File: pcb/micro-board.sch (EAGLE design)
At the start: 100 parts, among them IC1 STM32F401RET6U, IC2 LDS3985M33R, IC3 LDS3985M33R, IC4 HX711, IC5 TLV2462IP, J12 B2B-PH-K-S_LF__SN_, J3 Button / ADC Header, Q1 S8550, Q2 16MHz, U1 MCP73831.SOT23-5

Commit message: Updated the PCB board and schematic. In process of generally laying down components. Will be working on the design for next 1.5 hours.
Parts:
- added J18: DC Power, LinnesLab-Connectors:CONN_02
- added R34, R35: 1.5, LinnesLab-Passives:RESISTOR0603
- added U$2: TP3, LinnesLab-Connectors:PAD
- added U$3: TP4, LinnesLab-Connectors:PAD
- added U$4: TP5, LinnesLab-Connectors:PAD
- added U$5: TP6, LinnesLab-Connectors:PAD
- added U$6: TP1, LinnesLab-Connectors:PAD
- added U$7: TP0, LinnesLab-Connectors:PAD
- added U$8: TP2, LinnesLab-Connectors:PAD
- J14: value (none) -> Digital LED
- J15: value (none) -> Analog LED
- J16: value (none) -> HX711 LED
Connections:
- new net BOOT0: IC1.BOOT0, R11.1, U$4.1
- new net N$19: IC2.VO, R34.2
- net 3.3V: now also R34.1, U$7.1, U$8.1; no longer IC2.VO
- net 5V: now also J18.2
- net GND: now also J18.1
- net HXCLK_P: now also U$2.1
- net HXDATA_P: now also U$3.1
- net N$15: now also IC3.VO, R35.2; no longer IC1.BOOT0, R11.1
- net NRST: now also U$5.1
- net VDDA: now also R35.1, U$6.1; no longer IC3.VO
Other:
- note added: "3V3 TP0"
- note added: "HX711: TP2"
- note added: "Power Debug LEDs (J14-J16: Shorted = Enabled)"
- note added: "VDDA TP1"
- note removed: "Power Debug LEDs (Jumper-Enabled)"
- note removed: "TODO: Add 1.5 ohm resistor in series with power supply."
- note removed: "TODO: Discuss 5V connector mount"
- moved on the sheet: C15, C16, C17, C19, C2, C20, C22, C23, C24, C3, C7, C8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

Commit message: Updated the micro-board.brd file with power supply + basic polygons
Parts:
- J14: value Digital LED -> 3V3 LED
- J15: value Analog LED -> VDDA LED
- LED3: value Blue -> VDD
- LED4: value Blue -> VDDA
- R15: value 330 -> 470
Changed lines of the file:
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@@
 <part name="C12" library="LinnesLab-Passives" deviceset="CAPACITOR" device="0603" package3d_urn="urn:adsk.eagle:package:15661989/2" value="2.2uF"/>
 <part name="IC5" library="SamacSys_Parts" deviceset="TLV2462IP" device=""/>
-<part name="R15" library="LinnesLab-Passives" deviceset="RESISTOR" device="0603" package3d_urn="urn:adsk.eagle:package:15661944/2" value="330"/>
+<part name="R15" library="LinnesLab-Passives" deviceset="RESISTOR" device="0603" package3d_urn="urn:adsk.eagle:package:15661944/2" value="470"/>
 <part name="R16" library="LinnesLab-Passives" deviceset="RESISTOR" device="0603" package3d_urn="urn:adsk.eagle:package:15661944/2" value="470"/>
 <part name="R17" library="LinnesLab-Passives" deviceset="RESISTOR" device="0603" package3d_urn="urn:adsk.eagle:package:15661944/2" value="4.7k"/>
@@
 <part name="GND39" library="LinnesLab-Symbols" deviceset="GND" device=""/>
 <part name="C24" library="LinnesLab-Passives" deviceset="CAPACITOR" device="0603" package3d_urn="urn:adsk.eagle:package:15661989/2" value="0.1uF"/>
-<part name="J14" library="LinnesLab-Connectors" deviceset="CONN_02" device="" value="Digital LED"/>
+<part name="J14" library="LinnesLab-Connectors" deviceset="CONN_02" device="" value="3V3 LED"/>
 <part name="R24" library="LinnesLab-Passives" deviceset="RESISTOR" device="0603" package3d_urn="urn:adsk.eagle:package:15661944/2" value="470"/>
-<part name="LED3" library="LinnesLab-LED" deviceset="LED" device="0603" package3d_urn="urn:adsk.eagle:package:18593052/2" value="Blue"/>
+<part name="LED3" library="LinnesLab-LED" deviceset="LED" device="0603" package3d_urn="urn:adsk.eagle:package:18593052/2" value="VDD"/>
 <part name="GND40" library="LinnesLab-Symbols" deviceset="GND" device=""/>
 <part name="R25" library="LinnesLab-Passives" deviceset="RESISTOR" device="0603" package3d_urn="urn:adsk.eagle:package:15661944/2" value="470"/>
-<part name="LED4" library="LinnesLab-LED" deviceset="LED" device="0603" package3d_urn="urn:adsk.eagle:package:18593052/2" value="Blue"/>
+<part name="LED4" library="LinnesLab-LED" deviceset="LED" device="0603" package3d_urn="urn:adsk.eagle:package:18593052/2" value="VDDA"/>
 <part name="GND41" library="LinnesLab-Symbols" deviceset="GND" device=""/>
 <part name="R27" library="LinnesLab-Passives" deviceset="RESISTOR" device="0603" package3d_urn="urn:adsk.eagle:package:15661944/2" value="470"/>
@@
 <part name="R26" library="LinnesLab-Passives" deviceset="RESISTOR" device="0603" package3d_urn="urn:adsk.eagle:package:15661944/2" value="470"/>
 <part name="R28" library="LinnesLab-Passives" deviceset="RESISTOR" device="0603" package3d_urn="urn:adsk.eagle:package:15661944/2" value="1k"/>
-<part name="J15" library="LinnesLab-Connectors" deviceset="CONN_02" device="" value="Analog LED"/>
+<part name="J15" library="LinnesLab-Connectors" deviceset="CONN_02" device="" value="VDDA LED"/>
 <part name="J17" library="LinnesLab-Connectors" deviceset="CONN_03" device=""/>
 <part name="GND48" library="LinnesLab-Symbols" deviceset="GND" device=""/>

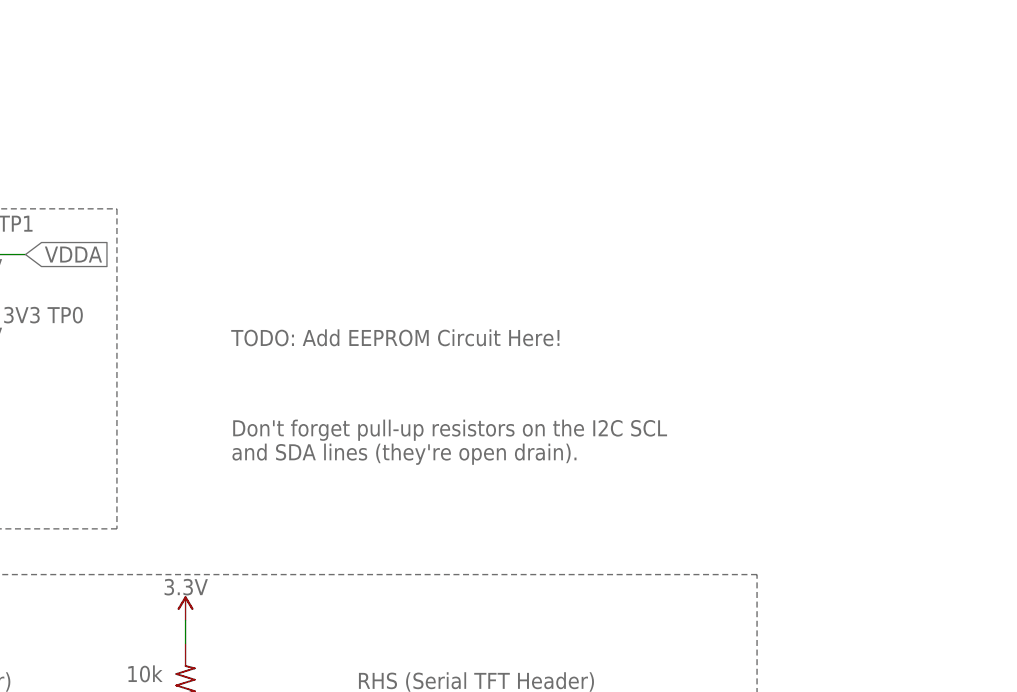
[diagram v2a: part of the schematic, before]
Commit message: Finished simplistic EEPROM routing on back of main board
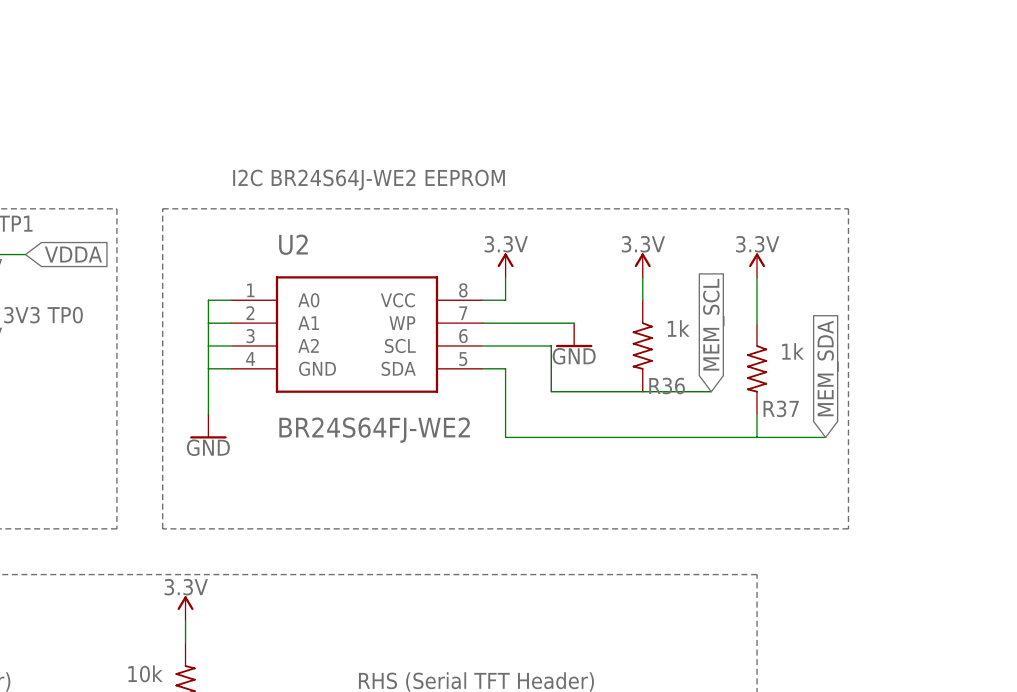
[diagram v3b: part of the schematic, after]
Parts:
- added R36, R37: 1k, LinnesLab-Passives:RESISTOR0603
- added U2: BR24S64FJ-WE2, I2C-EEPROM:BR24S64FJ-WE2
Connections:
- net 3.3V: now also R36.1, R37.1, U2.VCC
- net GND: now also U2.A0, U2.A1, U2.A2, U2.GND, U2.WP
- net MEM_SCL: now also R36.2, U2.SCL
- net MEM_SDA: now also R37.2, U2.SDA
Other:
- note added: "I2C BR24S64J-WE2 EEPROM"
- note removed: "Don't forget pull-up resistors on the I2C SCL and SDA lines (they're open drain)."
- note removed: "TODO: Add EEPROM Circuit Here!"
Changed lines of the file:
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@@
 <part name="SUPPLY33" library="LinnesLab-Symbols" deviceset="3.3V" device=""/>
 <part name="SUPPLY36" library="LinnesLab-Symbols" deviceset="3.3V" device=""/>
+<part name="U2" library="I2C-EEPROM" deviceset="BR24S64FJ-WE2" device=""/>
+<part name="GND53" library="LinnesLab-Symbols" deviceset="GND" device=""/>
+<part name="SUPPLY37" library="LinnesLab-Symbols" deviceset="3.3V" device=""/>
+<part name="GND54" library="LinnesLab-Symbols" deviceset="GND" device=""/>
+<part name="SUPPLY38" library="LinnesLab-Symbols" deviceset="3.3V" device=""/>
+<part name="R36" library="LinnesLab-Passives" deviceset="RESISTOR" device="0603" package3d_urn="urn:adsk.eagle:package:15661944/2" value="1k"/>
+<part name="R37" library="LinnesLab-Passives" deviceset="RESISTOR" device="0603" package3d_urn="urn:adsk.eagle:package:15661944/2" value="1k"/>
+<part name="SUPPLY39" library="LinnesLab-Symbols" deviceset="3.3V" device=""/>
 </parts>
 <sheets>
@@
 <text x="190.5" y="162.56" size="1.778" layer="95">D7-D0 unused</text>
 <text x="182.626" y="176.022" size="1.778" layer="95">TFT LCD 2.8" Adafruit RT Touchscreen</text>
-<text x="264.16" y="200.66" size="1.778" layer="95">TODO: Add EEPROM Circuit Here!</text>
-<text x="264.16" y="187.96" size="1.778" layer="95">Don't forget pull-up resistors on the I2C SCL
-and SDA lines (they're open drain).</text>
 <text x="4.826" y="33.528" size="1.778" layer="95">MCU to MAX7219</text>
 <text x="142.24" y="35.56" size="1.778" layer="95">Scope Probe
@@
 <text x="238.76" y="203.2" size="1.778" layer="95">3V3 TP0</text>
 <text x="231.14" y="213.36" size="1.778" layer="95">VDDA TP1</text>
+<wire x1="256.54" y1="215.9" x2="332.74" y2="215.9" width="0.1524" layer="95" style="shortdash"/>
+<wire x1="332.74" y1="215.9" x2="332.74" y2="180.34" width="0.1524" layer="95" style="shortdash"/>
+<wire x1="332.74" y1="180.34" x2="256.54" y2="180.34" width="0.1524" layer="95" style="shortdash"/>
+<wire x1="256.54" y1="180.34" x2="256.54" y2="215.9" width="0.1524" layer="95" style="shortdash"/>
+<text x="264.16" y="218.44" size="1.778" layer="95">I2C BR24S64J-WE2 EEPROM</text>
 </plain>
 <instances>
@@
 <instance part="SUPPLY36" gate="G$1" x="236.22" y="198.12" smashed="yes">
 <attribute name="VALUE" x="236.22" y="200.914" size="1.778" layer="96" align="bottom-center"/>
+</instance>
+<instance part="U2" gate="G$1" x="299.72" y="195.58" smashed="yes">
+<attribute name="NAME" x="269.24" y="210.82" size="2.1844" layer="95"/>
+<attribute name="VALUE" x="269.24" y="190.5" size="2.1844" layer="96"/>
+</instance>
+<instance part="GND53" gate="G$1" x="261.62" y="190.5" smashed="yes">
+<attribute name="VALUE" x="261.62" y="190.246" size="1.778" layer="96" align="top-center"/>
+</instance>
+<instance part="SUPPLY37" gate="G$1" x="294.64" y="208.28" smashed="yes">
+<attribute name="VALUE" x="294.64" y="211.074" size="1.778" layer="96" align="bottom-center"/>
+</instance>
+<instance part="GND54" gate="G$1" x="302.26" y="200.66" smashed="yes">
+<attribute name="VALUE" x="302.26" y="200.406" size="1.778" layer="96" align="top-center"/>
+</instance>
+<instance part="SUPPLY38" gate="G$1" x="309.88" y="208.28" smashed="yes">
+<attribute name="VALUE" x="309.88" y="211.074" size="1.778" layer="96" align="bottom-center"/>
+</instance>
+<instance part="R36" gate="G$1" x="309.88" y="200.66" smashed="yes" rot="R270">
+<attribute name="NAME" x="314.706" y="197.104" size="1.778" layer="95" rot="R180"/>
+<attribute name="VALUE" x="312.42" y="201.676" size="1.778" layer="96"/>
+</instance>
+<instance part="R37" gate="G$1" x="322.58" y="198.12" smashed="yes" rot="R270">
+<attribute name="NAME" x="327.406" y="194.564" size="1.778" layer="95" rot="R180"/>
+<attribute name="VALUE" x="325.12" y="199.136" size="1.778" layer="96"/>
+</instance>
+<instance part="SUPPLY39" gate="G$1" x="322.58" y="208.28" smashed="yes">
+<attribute name="VALUE" x="322.58" y="211.074" size="1.778" layer="96" align="bottom-center"/>
 </instance>
 </instances>
@@
 <wire x1="195.58" y1="73.66" x2="195.58" y2="68.58" width="0.1524" layer="91"/>
 <pinref part="GND52" gate="G$1" pin="GND"/>
+</segment>
+<segment>
+<pinref part="GND53" gate="G$1" pin="GND"/>
+<wire x1="261.62" y1="198.12" x2="261.62" y2="193.04" width="0.1524" layer="91"/>
+<pinref part="U2" gate="G$1" pin="GND"/>
+<wire x1="264.16" y1="198.12" x2="261.62" y2="198.12" width="0.1524" layer="91"/>
+<pinref part="U2" gate="G$1" pin="A2"/>
+<wire x1="261.62" y1="198.12" x2="261.62" y2="200.66" width="0.1524" layer="91"/>
+<wire x1="261.62" y1="200.66" x2="264.16" y2="200.66" width="0.1524" layer="91"/>
+<pinref part="U2" gate="G$1" pin="A1"/>
+<wire x1="264.16" y1="203.2" x2="261.62" y2="203.2" width="0.1524" layer="91"/>
+<wire x1="261.62" y1="203.2" x2="261.62" y2="200.66" width="0.1524" layer="91"/>
+<pinref part="U2" gate="G$1" pin="A0"/>
+<wire x1="261.62" y1="203.2" x2="261.62" y2="205.74" width="0.1524" layer="91"/>
+<wire x1="261.62" y1="205.74" x2="264.16" y2="205.74" width="0.1524" layer="91"/>
+</segment>
+<segment>
+<pinref part="GND54" gate="G$1" pin="GND"/>
+<pinref part="U2" gate="G$1" pin="WP"/>
+<wire x1="302.26" y1="203.2" x2="292.1" y2="203.2" width="0.1524" layer="91"/>
 </segment>
 </net>
@@
 <label x="76.2" y="124.46" size="1.778" layer="95" rot="R90" xref="yes"/>
 </segment>
+<segment>
+<pinref part="U2" gate="G$1" pin="SCL"/>
+<wire x1="292.1" y1="200.66" x2="299.72" y2="200.66" width="0.1524" layer="91"/>
+<pinref part="R36" gate="G$1" pin="2"/>
+<wire x1="299.72" y1="200.66" x2="299.72" y2="195.58" width="0.1524" layer="91"/>
+<wire x1="299.72" y1="195.58" x2="309.88" y2="195.58" width="0.1524" layer="91"/>
+<wire x1="309.88" y1="195.58" x2="317.5" y2="195.58" width="0.1524" layer="91"/>
+<label x="317.5" y="195.58" size="1.778" layer="95" rot="R90" xref="yes"/>
+</segment>
 </net>
 <net name="MEM_SDA" class="0">
@@
 <wire x1="73.66" y1="119.38" x2="73.66" y2="142.24" width="0.1524" layer="91"/>
 <label x="73.66" y="142.24" size="1.778" layer="95" rot="R90" xref="yes"/>
+</segment>
+<segment>
+<pinref part="U2" gate="G$1" pin="SDA"/>
+<wire x1="292.1" y1="198.12" x2="294.64" y2="198.12" width="0.1524" layer="91"/>
+<wire x1="294.64" y1="198.12" x2="294.64" y2="190.5" width="0.1524" layer="91"/>
+<wire x1="294.64" y1="190.5" x2="322.58" y2="190.5" width="0.1524" layer="91"/>
+<pinref part="R37" gate="G$1" pin="2"/>
+<wire x1="322.58" y1="190.5" x2="322.58" y2="193.04" width="0.1524" layer="91"/>
+<wire x1="322.58" y1="190.5" x2="330.2" y2="190.5" width="0.1524" layer="91"/>
+<label x="330.2" y="190.5" size="1.778" layer="95" rot="R90" xref="yes"/>
 </segment>
 </net>
@@
 <wire x1="236.22" y1="195.58" x2="236.22" y2="198.12" width="0.1524" layer="91"/>
 </segment>
-</net>
+<segment>
+<pinref part="U2" gate="G$1" pin="VCC"/>
+<pinref part="SUPPLY37" gate="G$1" pin="3.3V"/>
+<wire x1="292.1" y1="205.74" x2="294.64" y2="205.74" width="0.1524" layer="91"/>
+<wire x1="294.64" y1="205.74" x2="294.64" y2="208.28" width="0.1524" layer="91"/>
+</segment>
+<segment>
+<pinref part="SUPPLY38" gate="G$1" pin="3.3V"/>
+<wire x1="309.88" y1="205.74" x2="309.88" y2="208.28" width="0.1524" layer="91"/>
+<pinref part="R36" gate="G$1" pin="1"/>
+</segment>
+<segment>
+<pinref part="SUPPLY39" gate="G$1" pin="3.3V"/>
+<pinref part="R37" gate="G$1" pin="1"/>
+<wire x1="322.58" y1="208.28" x2="322.58" y2="203.2" width="0.1524" layer="91"/>
+</segment>
+</net>

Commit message: Updated TFT right-side header, debug headers, and routing
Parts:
- added C32: 0.1uF, LinnesLab-Passives:CAPACITOR0603
- added R38, R39: 10k, LinnesLab-Passives:RESISTOR0603
- R27: value 470 -> 1k
- renumbered J10 to TFT
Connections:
- net N$8 renamed VCAP1
- new net IM2: R38.2, SV2.5
- new net IM3: R39.2, SV2.6
- net 3.3V: now also C32.2, R38.1, R39.1, R6.1
- net GND: now also C32.1; no longer R6.1
- net NC_MISO: now also J6.4; no longer J6.5
- net SS_CS: now also J6.2; no longer J6.3
- net SS_MOSI: now also J6.5; no longer J6.4
- net SS_SCK: now also J6.3; no longer J6.2
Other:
- moved on the sheet: R36

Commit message: Incremental commit of changes made
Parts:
- added C33: 0.1uF, LinnesLab-Passives:CAPACITOR0603
- added C34: 10uF, LinnesLab-Passives:CAPACITOR0603
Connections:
- net 3.3V: now also C33.1, C34.1
- net GND: now also C33.2, C34.2
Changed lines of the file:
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@@
 <setting verticaltext="up"/>
 </settings>
-<grid distance="0.1" unitdist="inch" unit="inch" style="lines" multiple="1" display="yes" altdistance="0.01" altunitdist="inch" altunit="inch"/>
+<grid distance="0.01" unitdist="inch" unit="inch" style="lines" multiple="1" display="yes" altdistance="0.01" altunitdist="inch" altunit="inch"/>
 <layers>
 <layer number="1" name="Top" color="4" fill="1" visible="no" active="no"/>
@@
 <part name="R39" library="LinnesLab-Passives" deviceset="RESISTOR" device="0603" package3d_urn="urn:adsk.eagle:package:15661944/2" value="10k"/>
 <part name="SUPPLY40" library="LinnesLab-Symbols" deviceset="3.3V" device=""/>
+<part name="C33" library="LinnesLab-Passives" deviceset="CAPACITOR" device="0603" package3d_urn="urn:adsk.eagle:package:15661989/2" value="0.1uF"/>
+<part name="C34" library="LinnesLab-Passives" deviceset="CAPACITOR" device="0603" package3d_urn="urn:adsk.eagle:package:15661989/2" value="10uF"/>
 </parts>
 <sheets>
@@
 <wire x1="363.22" y1="71.12" x2="363.22" y2="7.62" width="0.1524" layer="95" style="shortdash"/>
 <wire x1="363.22" y1="7.62" x2="414.02" y2="7.62" width="0.1524" layer="95" style="shortdash"/>
-<wire x1="332.74" y1="71.12" x2="358.14" y2="71.12" width="0.1524" layer="95" style="shortdash"/>
+<wire x1="330.2" y1="71.12" x2="358.14" y2="71.12" width="0.1524" layer="95" style="shortdash"/>
 <wire x1="358.14" y1="71.12" x2="358.14" y2="38.1" width="0.1524" layer="95" style="shortdash"/>
-<wire x1="358.14" y1="38.1" x2="332.74" y2="38.1" width="0.1524" layer="95" style="shortdash"/>
-<wire x1="332.74" y1="38.1" x2="332.74" y2="71.12" width="0.1524" layer="95" style="shortdash"/>
+<wire x1="358.14" y1="38.1" x2="330.2" y2="38.1" width="0.1524" layer="95" style="shortdash"/>
+<wire x1="330.2" y1="38.1" x2="330.2" y2="71.12" width="0.1524" layer="95" style="shortdash"/>
 <wire x1="327.66" y1="78.74" x2="327.66" y2="0" width="0.1524" layer="95" style="shortdash"/>
 <wire x1="327.66" y1="0" x2="553.72" y2="0" width="0.1524" layer="95" style="shortdash"/>
@@
 </instance>
 <instance part="C15" gate="G$1" x="339.09" y="53.34" smashed="yes">
-<attribute name="NAME" x="340.614" y="56.261" size="1.778" layer="95"/>
-<attribute name="VALUE" x="340.614" y="51.181" size="1.778" layer="96"/>
+<attribute name="NAME" x="339.852" y="56.261" size="1.778" layer="95"/>
+<attribute name="VALUE" x="339.852" y="51.181" size="1.778" layer="96"/>
 </instance>
 <instance part="C16" gate="G$1" x="349.25" y="53.34" smashed="yes">
-<attribute name="NAME" x="350.774" y="56.261" size="1.778" layer="95"/>
-<attribute name="VALUE" x="350.774" y="51.181" size="1.778" layer="96"/>
+<attribute name="NAME" x="344.424" y="56.261" size="1.778" layer="95"/>
+<attribute name="VALUE" x="343.408" y="48.895" size="1.778" layer="96"/>
 </instance>
 <instance part="GND18" gate="G$1" x="344.17" y="45.72" smashed="yes">
@@
 <attribute name="VALUE" x="246.38" y="155.194" size="1.778" layer="96" align="bottom-center"/>
 </instance>
+<instance part="C33" gate="G$1" x="334.01" y="53.34" smashed="yes">
+<attribute name="NAME" x="332.994" y="58.801" size="1.778" layer="95"/>
+<attribute name="VALUE" x="332.994" y="46.101" size="1.778" layer="96"/>
+</instance>
+<instance part="C34" gate="G$1" x="354.076" y="53.34" smashed="yes">
+<attribute name="NAME" x="351.536" y="61.341" size="1.778" layer="95"/>
+<attribute name="VALUE" x="351.536" y="46.101" size="1.778" layer="96"/>
+</instance>
 </instances>
 <busses>
@@
 <wire x1="349.25" y1="48.26" x2="344.17" y2="48.26" width="0.1524" layer="91"/>
 <junction x="344.17" y="48.26"/>
+<pinref part="C33" gate="G$1" pin="2"/>
+<wire x1="334.01" y1="50.8" x2="334.01" y2="48.26" width="0.1524" layer="91"/>
+<wire x1="334.01" y1="48.26" x2="339.09" y2="48.26" width="0.1524" layer="91"/>
+<pinref part="C34" gate="G$1" pin="2"/>
+<wire x1="354.076" y1="50.8" x2="354.076" y2="48.26" width="0.1524" layer="91"/>
+<wire x1="354.076" y1="48.26" x2="349.25" y2="48.26" width="0.1524" layer="91"/>
 </segment>
 <segment>
@@
 <wire x1="344.17" y1="60.96" x2="344.17" y2="63.5" width="0.1524" layer="91"/>
 <junction x="344.17" y="60.96"/>
-</segment>
-<segment>
+<pinref part="C33" gate="G$1" pin="1"/>
+<wire x1="334.01" y1="60.96" x2="334.01" y2="58.42" width="0.1524" layer="91"/>
+<wire x1="334.01" y1="60.96" x2="339.09" y2="60.96" width="0.1524" layer="91"/>
+<pinref part="C34" gate="G$1" pin="1"/>
+<wire x1="354.076" y1="58.42" x2="354.076" y2="60.96" width="0.1524" layer="91"/>
+<wire x1="354.076" y1="60.96" x2="349.25" y2="60.96" width="0.1524" layer="91"/>
+</segment>
+<segment>

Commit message: Updated the initial revision of the PCB + PDFs of layout
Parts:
- removed C34: 10uF, LinnesLab-Passives:CAPACITOR0603
- added PWR: (no value), LinnesLab-Connectors:CONN_02
- added R40, R41, R42, R43: 20, LinnesLab-Passives:RESISTOR0603
- C29: value 0.1uF -> 10uF
- renumbered Q2 to X1, S1 to NRST, SJ1 to 80HZ, SJ2 to 10HZ, TFT to SPI
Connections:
- new net GND-ISO: C15.2, C16.2, C17.1, C29.2, C33.2, IC4.AGND, IC4.XI, J5.1, J7.3, LED6.C, R27.1, R4.1
- new net VDD: C15.1, C16.1, C29.1, C33.1, IC4.DVDD, IC4.VSUP, J16.2, J5.4, Q1.E, R28.1, U$8.1
- new net VIN: J12.1, PWR.1
- new net X+_NC: SV1.12
- new net X-_NC: SV1.10
- new net Y+_NC: SV1.11
- new net Y-_NC: SV1.9
- new net _HXCLK: J5.3, R32.2
- new net _HXDATA: J5.2, R33.2
- new net _NC_MISO: IC1.PA6, R42.2
- new net _SS_CS: IC1.PA4, R40.2
- new net _SS_MOSI: IC1.PA7, R43.2
- new net _SS_SCK: IC1.PA5, R41.2
- net 3.3V: no longer C15.1, C16.1, C29.1, C33.1, C34.1, IC4.DVDD, IC4.VSUP, J16.2, J5.4, Q1.E, R14.2, R28.1, U$8.1
- net GND: now also R14.2; no longer C15.2, C16.2, C17.1, C29.2, C33.2, C34.2, IC4.AGND, IC4.XI, J5.1, J7.3, LED6.C, R27.1, R4.1
- net HXCLK: no longer J5.3, R32.2
- net HXDATA: no longer J5.2, R33.2
- net NC_MISO: now also R42.1; no longer IC1.PA6
- net SS_CS: now also R40.1; no longer IC1.PA4
- net SS_MOSI: now also R43.1; no longer IC1.PA7
- net SS_SCK: now also R41.1; no longer IC1.PA5
- net V_BATT: now also PWR.2; no longer J12.1
- net X+: no longer SV1.12
- net X-: no longer SV1.10
- net Y+: no longer SV1.11
- net Y-: no longer SV1.9
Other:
- note added: "HX711: TP0"
- note removed: "HX711: TP2"
- moved on the sheet: C29, J12, R14
